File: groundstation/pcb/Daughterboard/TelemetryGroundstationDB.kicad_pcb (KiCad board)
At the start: 2 copper layers, 100 x 75 mm, 32 parts, among them J1 RFPC-SMA27-F, J2 ICD15S13E4GV00LF, M1 M4 Mounting Hole, M2 M4 Mounting Hole, M3 M4 Mounting Hole, M4 M4 Mounting Hole, U1 RC1780HP-RC232

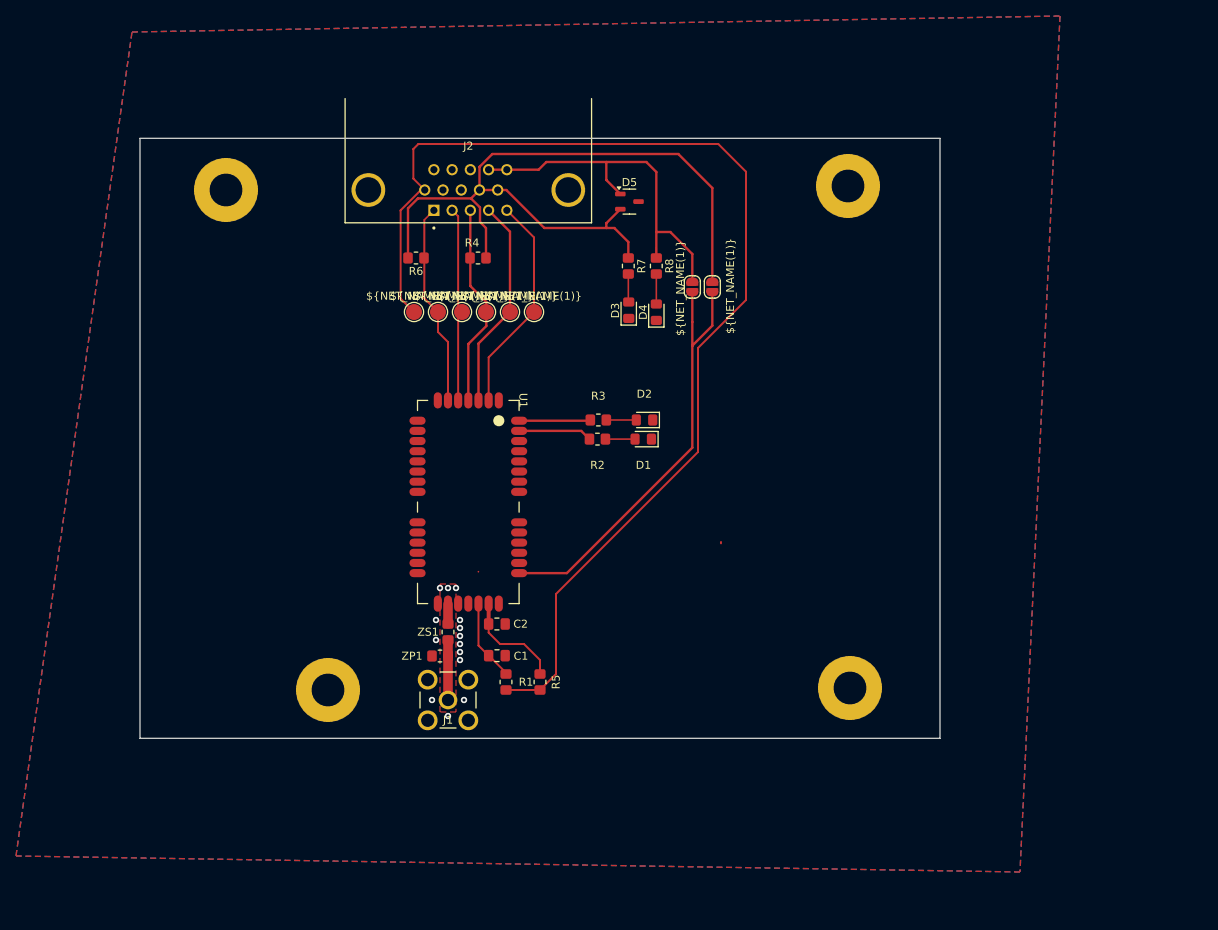
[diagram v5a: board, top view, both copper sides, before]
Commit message: add Silkscreen and dimesnion of the pcb
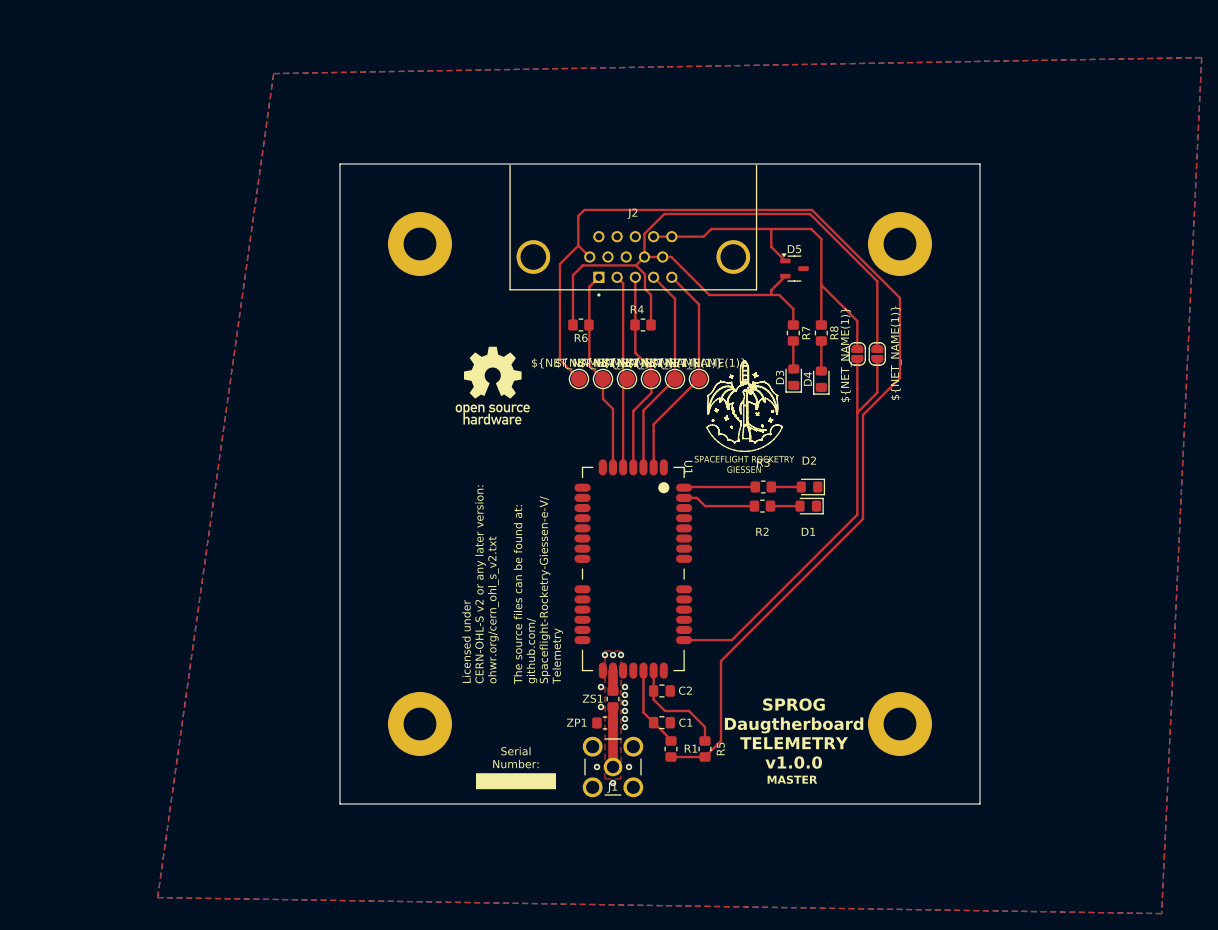
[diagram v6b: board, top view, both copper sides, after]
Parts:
- moved M3 25.2 mm to (-30.0, -30.0)
- moved C1 22.3 mm to (0.24, 29.8)
- moved C2 22.3 mm to (0.24, 25.9)
- moved D1 22.3 mm to (18.5, 2.77)
- moved D2 22.3 mm to (18.7, 0.38)
- moved D3 22.3 mm to (16.7, -13.3)
- moved D4 22.3 mm to (20.2, -13.1)
- moved D5 22.3 mm to (16.8, -26.9)
- moved J1 22.3 mm to (-5.88, 35.4)
- moved J2 22.3 mm to (-3.33, -28.4)
- moved JP1 22.3 mm to (24.7, -16.2)
- moved JP2 22.3 mm to (27.2, -16.2)
- moved R1 22.3 mm to (1.38, 33.1)
- moved R2 22.3 mm to (12.8, 2.77)
- moved R3 22.3 mm to (12.9, 0.38)
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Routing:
- net RST: track 146.5 -> 141.8 mm
- net +3V3: track 110.3 -> 109.1 mm
- net Net-(U1-D2): track 8.92 -> 9.55 mm
- net +5V: track 48.0 -> 47.4 mm
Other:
- board size 100 x 75 mm -> 80 x 80 mm
- board text added: "Licensed under CERN-OHL-S v2 or any later version: ohwr.org/cern_ohl_s_v2.txt The source files can be found at: github.com/ Spaceflight-Rocketry-Giessen-e-V/ Telemetry"
- board text added: "MASTER"
- board text added: "SPACEFLIGHT ROCKETRY GIESSEN"
- board text added: "SPROG Daughterboard TELEMETRY v1.0.0"
- board text added: "SPROG Daugtherboard TELEMETRY v1.0.0"
- board text added: "Serial Number:"

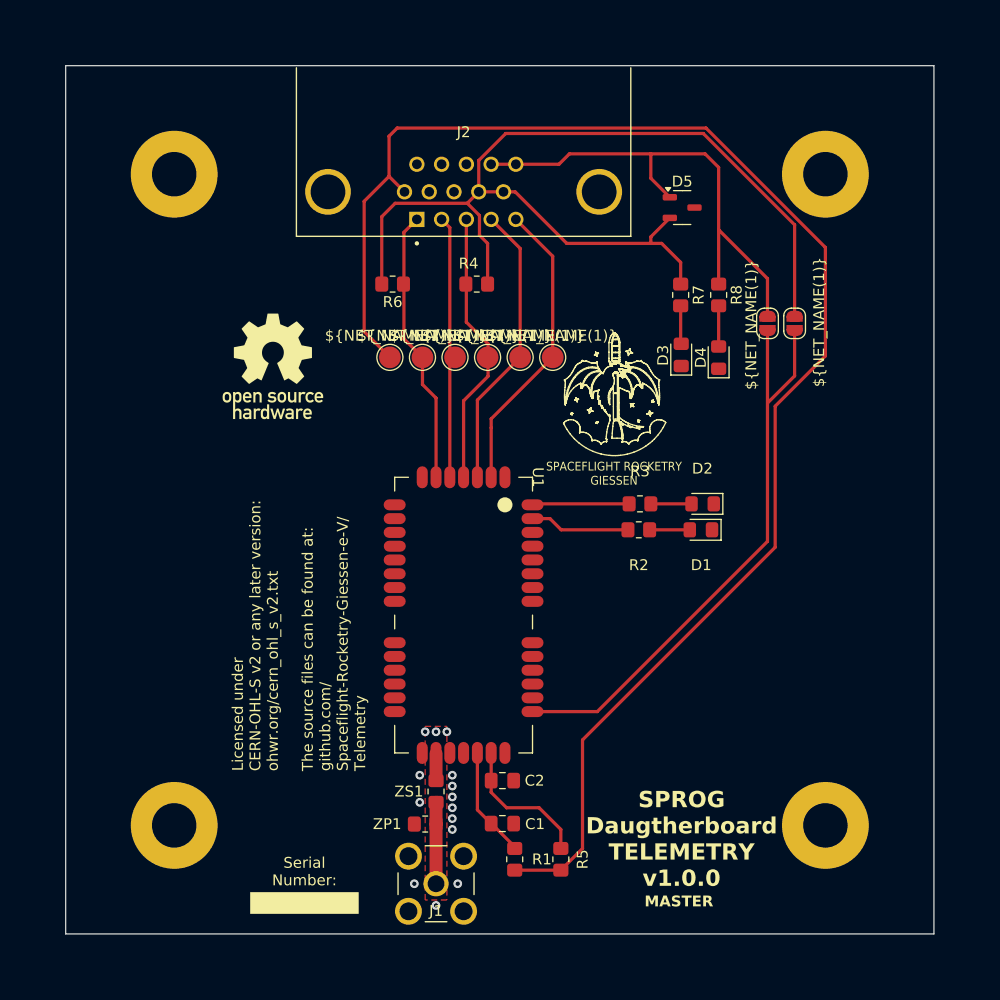
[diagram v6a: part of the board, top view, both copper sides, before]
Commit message: change dim to 40x70
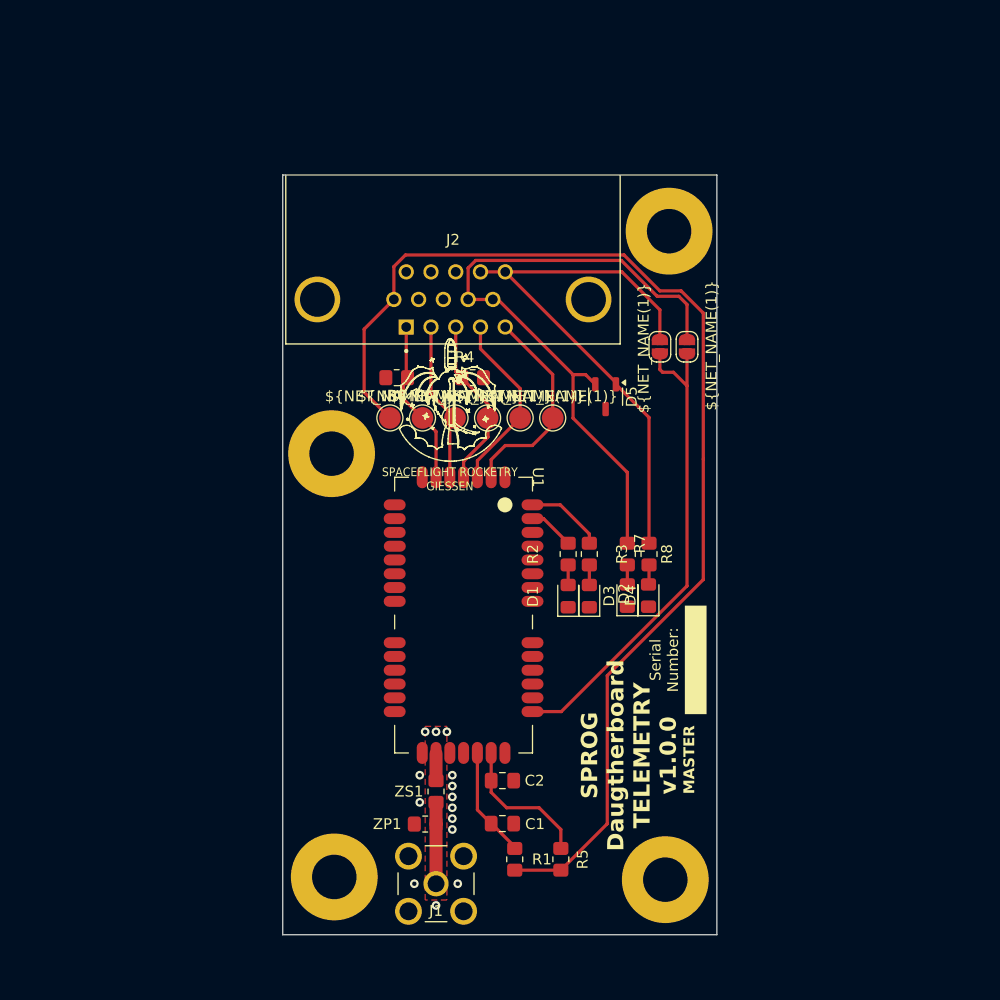
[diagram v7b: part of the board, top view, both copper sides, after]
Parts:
- moved M3 29.6 mm to (-15.5, -4.25)
- moved R8 24.7 mm to (13.8, 5.00)
- moved R7 24.4 mm to (11.8, 5.00)
- moved D4 22.9 mm to (13.7, 8.82)
- moved D3 22.7 mm to (11.8, 8.82)
- moved D5 18.8 mm to (9.75, -9.50), turned to -90 degrees
- moved M1 15.6 mm to (15.2, 35.0)
- moved M4 15.5 mm to (-15.2, 34.8)
- moved M2 15.3 mm to (15.6, -24.8)
- moved D1 13.7 mm to (6.30, 8.88), turned to 90 degrees
- moved D2 13.5 mm to (8.25, 8.88), turned to 90 degrees
- moved JP1 10.1 mm to (14.8, -14.1)
- moved JP2 10.1 mm to (17.2, -14.1)
- moved J2 9.96 mm to (-4.32, -18.5)
- moved R4 8.63 mm to (-2.50, -11.2)
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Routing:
- net +3V3: track 109.1 -> 74.4 mm
- net RST: track 141.8 -> 108.3 mm
- net TX: track 25.5 -> 15.5 mm
- net RTS: track 26.5 -> 17.0 mm
- net CFG: track 26.0 -> 16.5 mm
- net Net-(JP1-B): track 55.5 -> 46.2 mm
- net RX: track 24.1 -> 15.1 mm
- net CTS: track 28.1 -> 19.5 mm
- net Net-(U1-D1): track 9.42 -> 4.22 mm
- net +5V: track 47.4 -> 51.2 mm
- net Net-(U1-D2): track 9.55 -> 7.36 mm
- net Net-(D4-A): track 3.75 -> 1.82 mm
- net Net-(D2-A): track 3.75 -> 1.85 mm
- net Net-(D1-A): track 3.70 -> 1.85 mm
- net Net-(D3-A): track 3.52 -> 1.87 mm
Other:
- board size 80 x 80 mm -> 40 x 70 mm

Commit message: finalized design of daughterbaord
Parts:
- moved R8 1.25 mm to (12.5, 5.00)
- moved D3 1.20 mm to (10.6, 8.88)
- moved D4 1.20 mm to (12.5, 8.88)
- moved R7 1.20 mm to (10.6, 5.00)
- moved M4 0.99 mm to (-15.6, 35.7)
- moved M2 0.77 mm to (15.6, -25.5)
- moved M1 0.76 mm to (15.6, 35.7)
- moved M3 0.10 mm to (-15.6, -4.25)
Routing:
- net +3V3: track 74.4 -> 153.1 mm
- net Net-(JP1-B): track 46.2 -> 49.0 mm
- net RST: track 108.3 -> 109.6 mm
- net +5V: track 51.2 -> 50.7 mm
- net GND: vias 14 -> 15
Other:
- board text added: "SPROG e.V. Daugtherboard Telemetry v1.0.0"
- board text removed: "MASTER"
- board text removed: "SPROG Daughterboard TELEMETRY v1.0.0"
- board text removed: "SPROG Daugtherboard TELEMETRY v1.0.0"
